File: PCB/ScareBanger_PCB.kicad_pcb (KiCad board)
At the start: 2 copper layers, 84.4 x 56.1 mm, 27 parts, among them J1 RJ45, J16 Conn_01x10_Female - SAINSMART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, J17 Screw_Terminal_01x10 - HILETG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, J2 1757271, J3 Screw_Terminal_01x06, J4 Barrel_Jack_Switch, J5 AudioJack2_Ground, J6 Screw_Terminal_01x06, J7 Screw_Terminal_01x06, J8 Conn_01x04_Female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

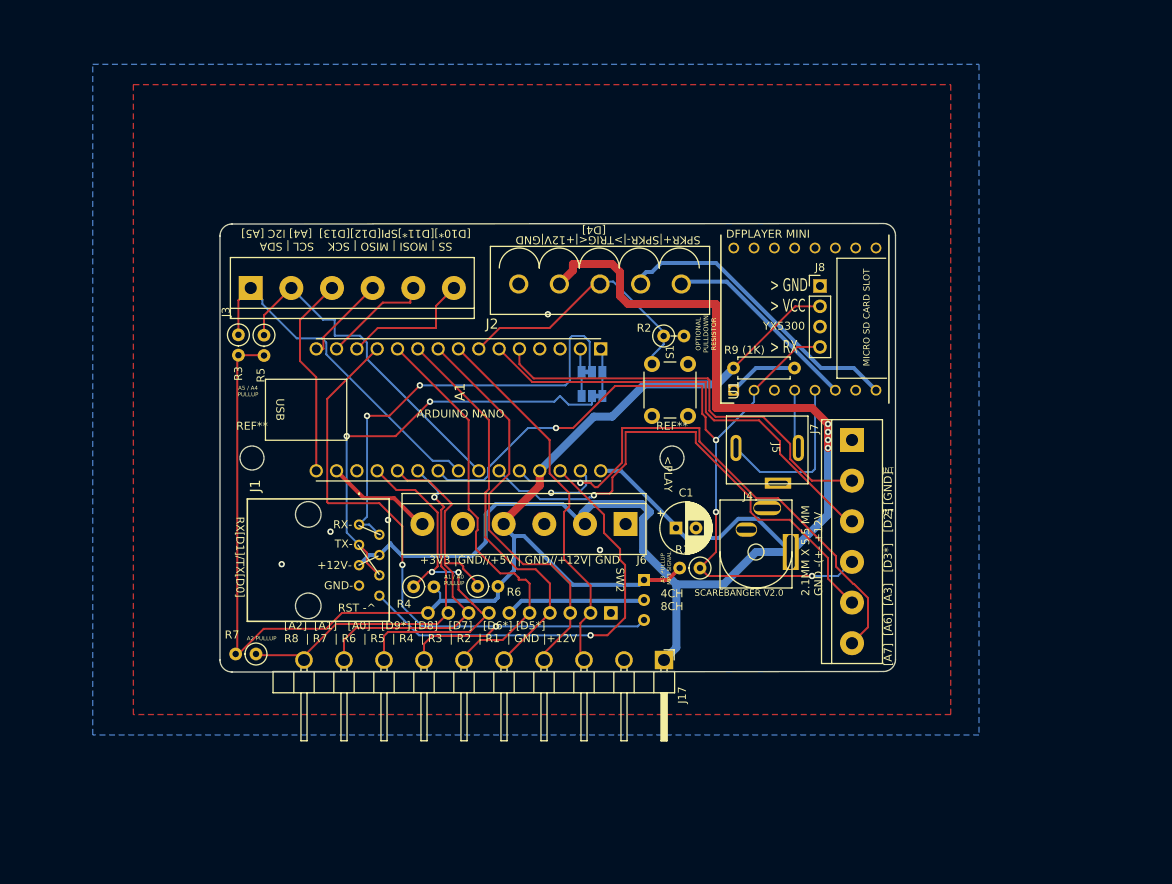
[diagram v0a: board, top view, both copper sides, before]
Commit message: added signal cap
added capacitor for signal wire, and  changed the main 12v trace to be 2mm wide
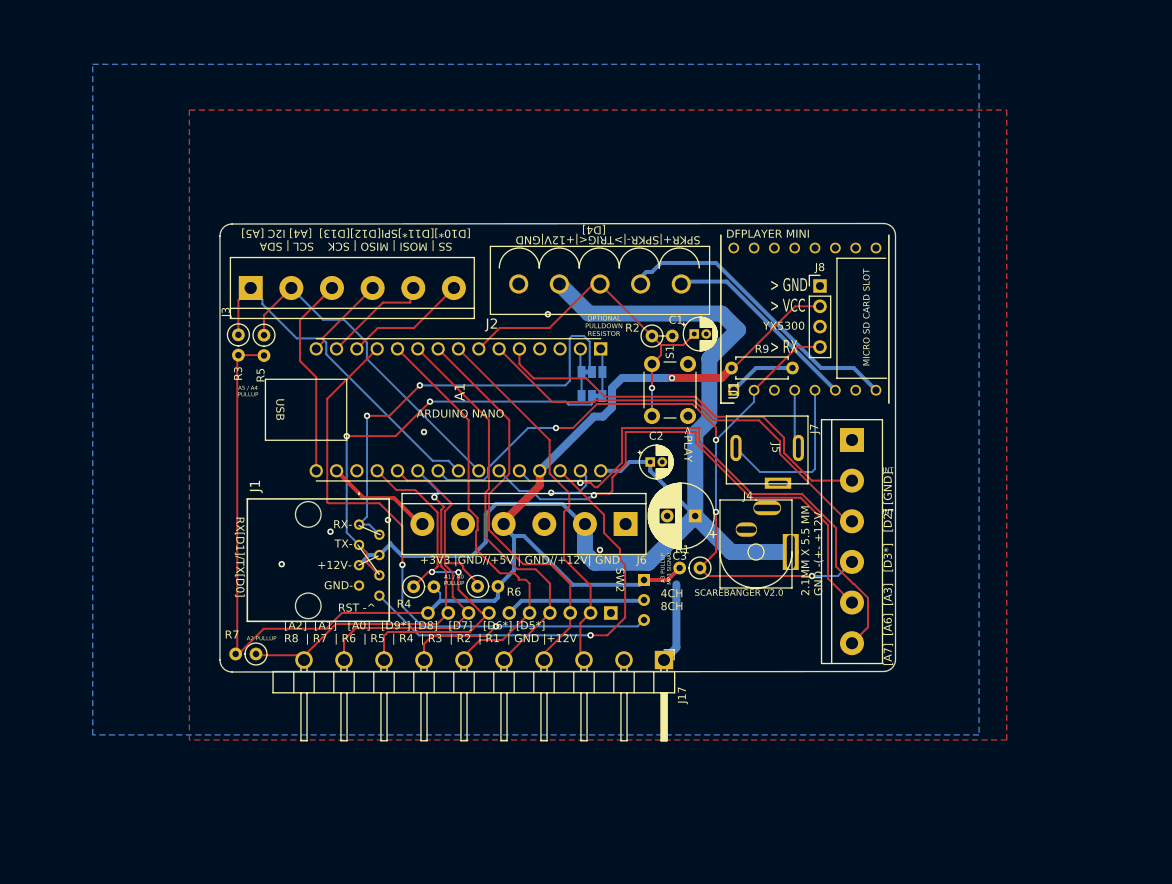
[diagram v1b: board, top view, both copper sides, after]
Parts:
- removed R9 (1K): 1K, Resistor_THT:R_Axial_DIN0207_L6.3mm_D2.5mm_P7.62mm_Horizontal
- removed REF** (x2): MountingHole_3mm, MountingHole:MountingHole_3mm
- added C2: 1uF, Capacitor_THT:CP_Radial_D4.0mm_P1.50mm, F.Cu at (154.8, 115.8)
- added C3: 470uF 50V, Capacitor_THT:CP_Radial_D8.0mm_P3.50mm, F.Cu at (160.4, 122.5)
- added R9: 1K, Resistor_THT:R_Axial_DIN0207_L6.3mm_D2.5mm_P7.62mm_Horizontal, F.Cu at (164.9, 104.0)
- C1: value 180uF -> 1uF; footprint Capacitor_THT:CP_Radial_D6.3mm_P2.50mm -> Capacitor_THT:CP_Radial_D4.0mm_P1.50mm
- moved C1 24.4 mm to (160.3, 99.8)
- moved R2 1.46 mm to (155.0, 100.0)
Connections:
- C1 pad 1: +12V -> Net-(A1-Pad7)
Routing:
- net +12V: track 187.2 -> 145.7 mm, vias 4 -> 0
- net Net-(A1-Pad7): track 32.8 -> 43.0 mm, vias 0 -> 1
- net Net-(A1-Pad22): track 102.0 -> 98.2 mm
- net Net-(A1-Pad5): track 52.9 -> 50.7 mm
- net Net-(A1-Pad26): track 67.0 -> 69.1 mm
- net Net-(A1-Pad6): track 56.2 -> 54.1 mm
- net Net-(A1-Pad13): track 16.9 -> 15.3 mm
- net Net-(A1-Pad25): track 64.6 -> 65.9 mm
- net +5V: track 165.9 -> 167.1 mm, vias 0 -> 1
- net Net-(A1-Pad24): track 42.6 -> 41.4 mm
- net Net-(J1-Pad3): track 53.3 -> 52.7 mm
- net Net-(A1-Pad15): track 11.1 -> 10.5 mm
- net (no net): vias 0 -> 1

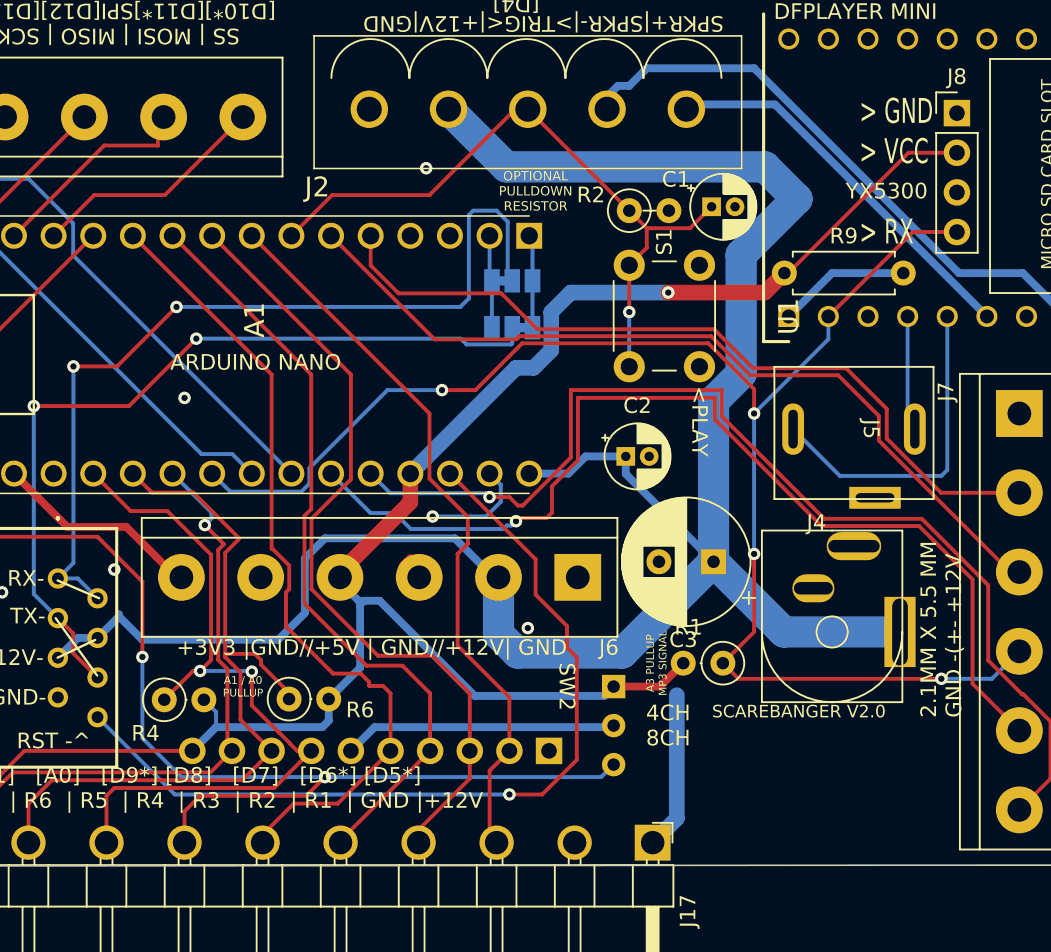
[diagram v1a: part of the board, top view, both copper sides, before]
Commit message: corrected some wire routing
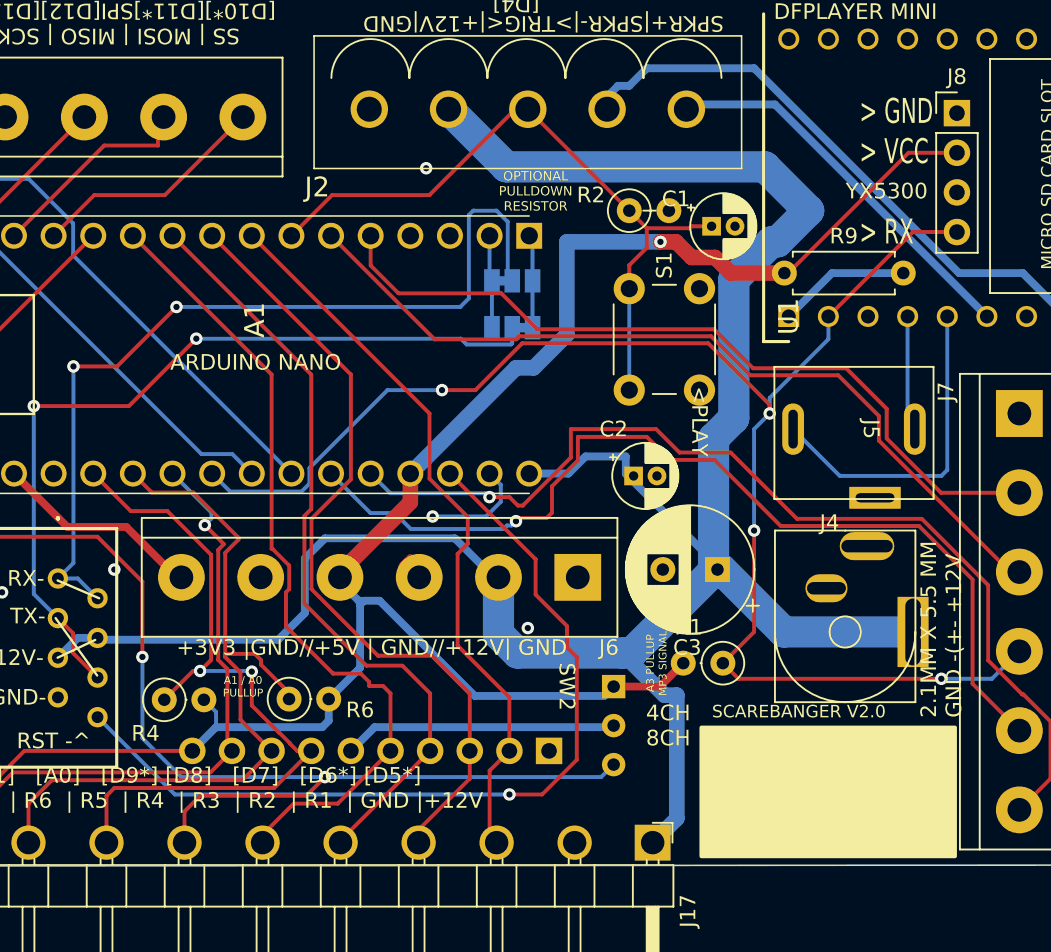
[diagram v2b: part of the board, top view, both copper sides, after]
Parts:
- moved S1 1.50 mm to (155.0, 111.5)
- moved C2 1.35 mm to (155.3, 117.0)
- moved C1 1.25 mm to (160.3, 101.0)
- moved J4 0.84 mm to (168.8, 127.0)
- moved C3 0.56 mm to (160.7, 123.0)
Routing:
- net +12V: track 145.7 -> 150.6 mm
- net Net-(A1-Pad26): track 69.1 -> 64.6 mm
- net Net-(A1-Pad25): track 65.9 -> 61.6 mm
- net +5V: track 167.1 -> 170.4 mm
- net Net-(A1-Pad7): track 43.0 -> 44.0 mm, vias 1 -> 0
- net (no net): vias 1 -> 0

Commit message: 4 layer update
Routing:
- net +12V: track 150.6 -> 34.7 mm
- net +5V: track 170.4 -> 127.4 mm, vias 1 -> 0
- net +3.3V: track 13.2 -> 0.00 mm
- net GND: track 7.58 -> 3.51 mm, vias 6 -> 5
- net Net-(A1-Pad26): vias 1 -> 0
- net Net-(A1-Pad25): vias 1 -> 0
- net Net-(A1-Pad22): vias 4 -> 3
- added copper zone on In2.Cu, net +12V
- added copper zone on In2.Cu, net +3.3V
- added copper zone on In2.Cu, net +5V
- added copper zone on In1.Cu, net GND
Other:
- copper layers 2 -> 4
- board text added: "V-PLAY"
- board text removed: "<PLAY"
